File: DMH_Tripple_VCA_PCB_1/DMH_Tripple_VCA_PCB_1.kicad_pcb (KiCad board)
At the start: 2 copper layers, 48 x 175 mm, 88 parts, among them J1 TS_Jack_6.35mm_Sw, J10 TS_Jack_6.35mm_Sw, J100 IDC_02x05, J2 TS_Jack_6.35mm_Sw, J200 IDC_02x05, J3 TS_Jack_6.35mm_Sw, J4 TS_Jack_6.35mm_Sw, J5 TS_Jack_6.35mm_Sw, J50 Conn_01x06, J6 TS_Jack_6.35mm_Sw, J60 Conn_01x06, J7 TS_Jack_6.35mm_Sw, J70 Conn_01x06, J8 TS_Jack_6.35mm_Sw, J9 TS_Jack_6.35mm_Sw, Q1 BC548, Q2 BC548, Q3 BC548, Q4 BC548, Q5 BC548, Q6 BC548, U1 TL074, U2 TL074

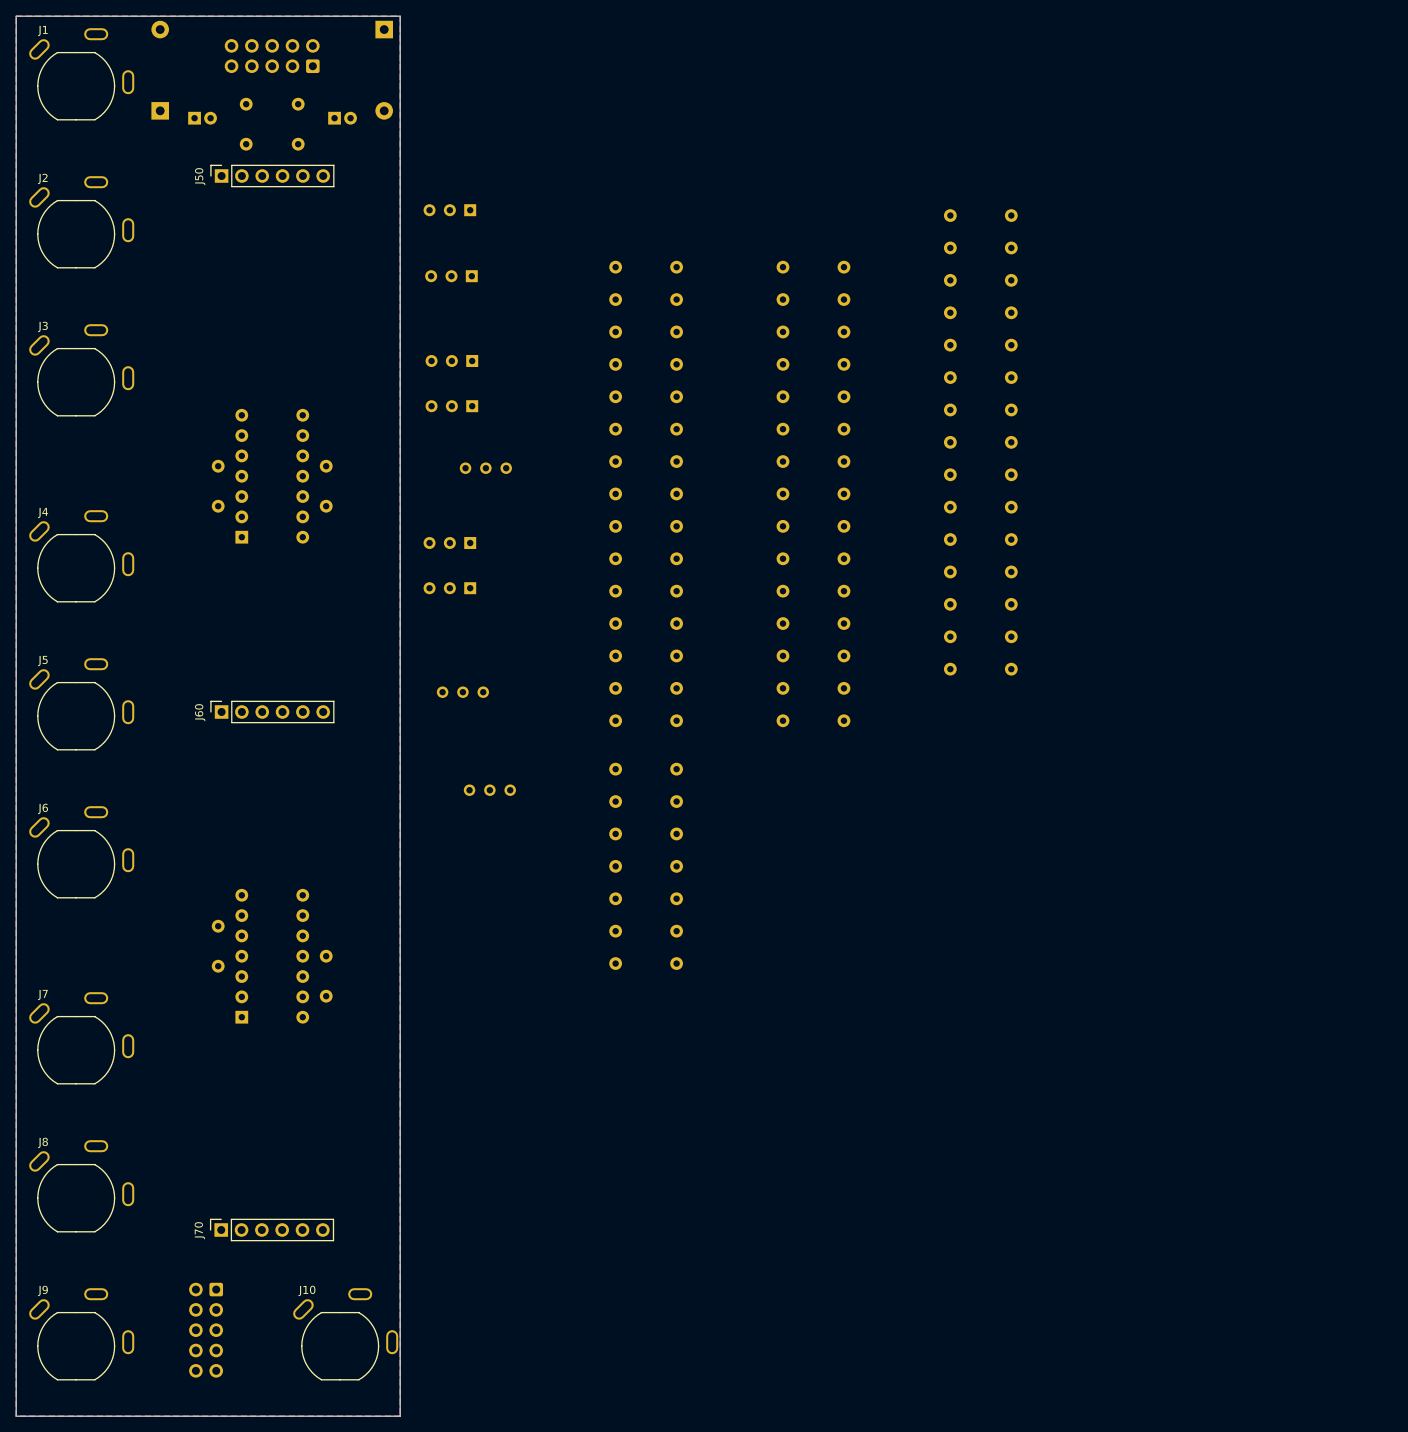
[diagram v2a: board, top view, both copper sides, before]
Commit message: PCB 1 Component placement done
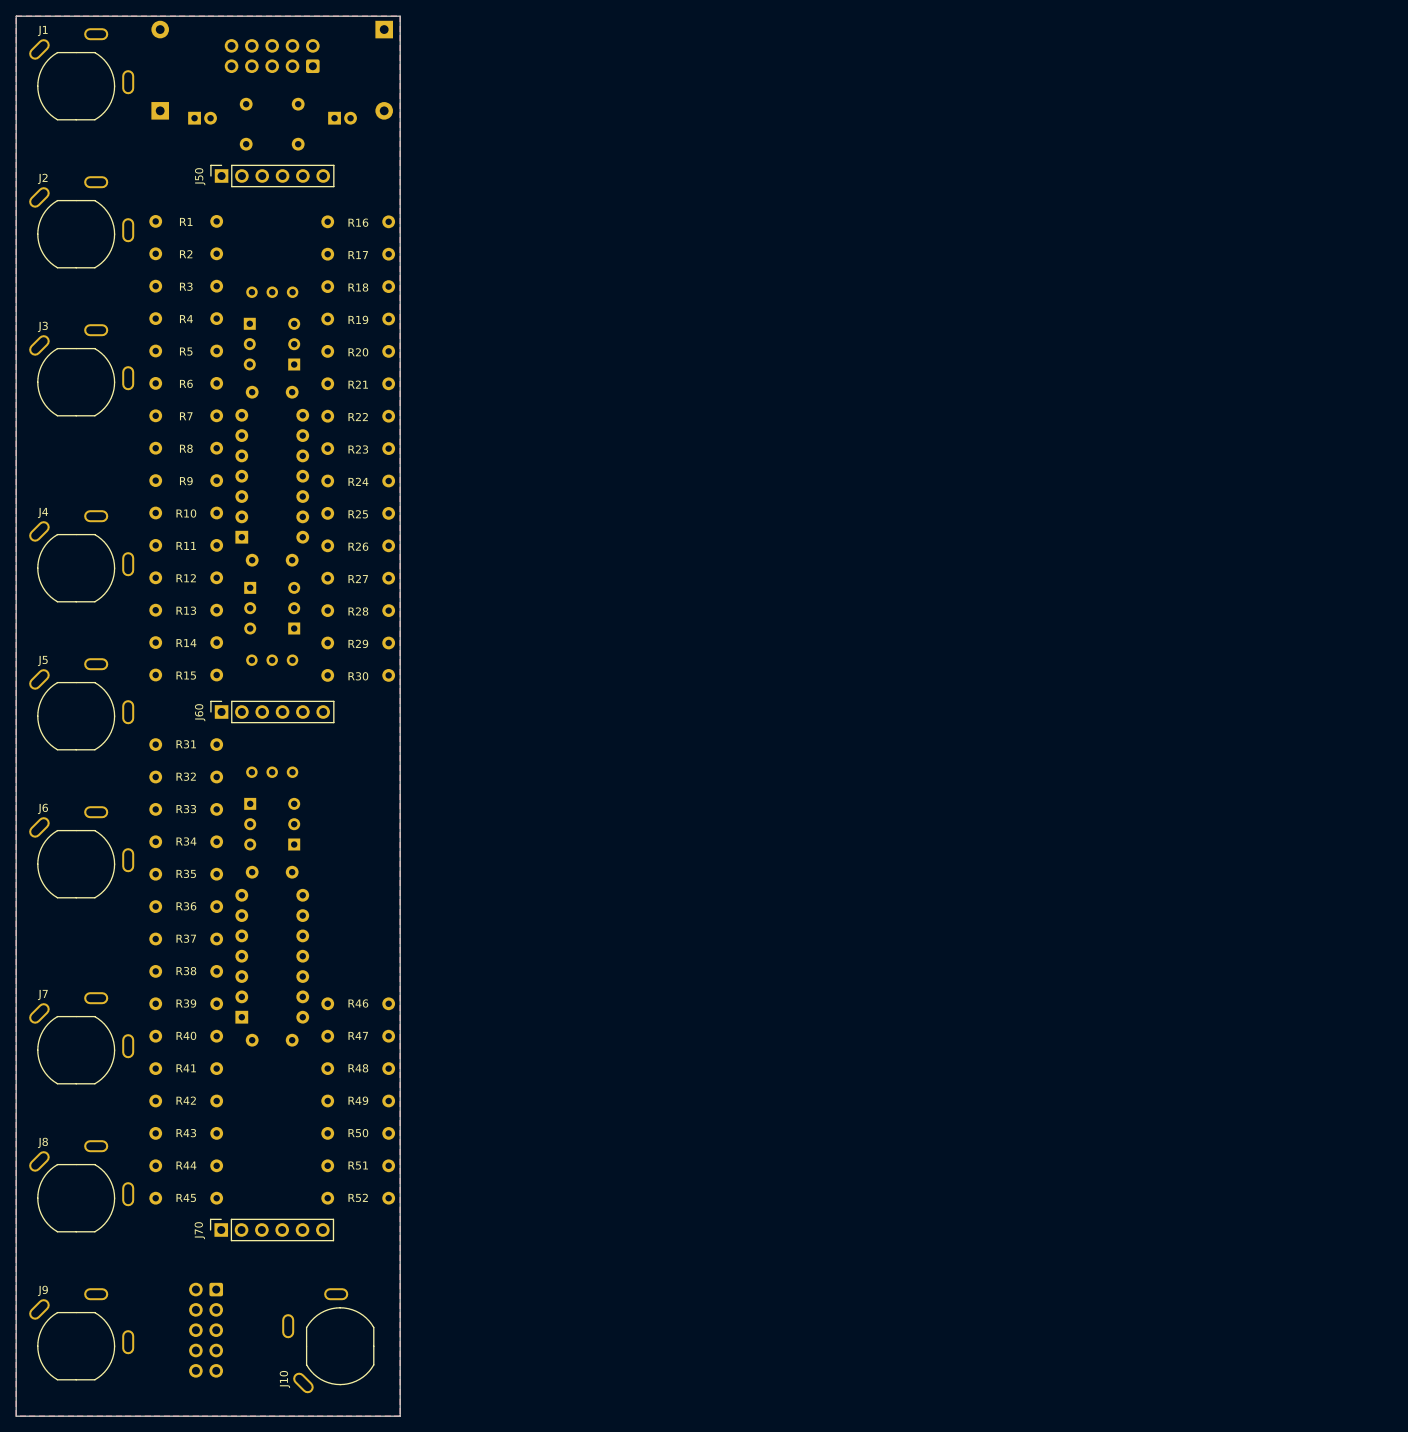
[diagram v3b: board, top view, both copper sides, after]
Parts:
- moved R35 104.7 mm to (68.4, 149.8), turned to 0 degrees
- moved R1 99.3 mm to (76.1, 68.2)
- moved R10 99.3 mm to (76.1, 104.6)
- moved R11 99.3 mm to (76.1, 108.7)
- moved R12 99.3 mm to (76.1, 112.7)
- moved R13 99.3 mm to (76.1, 116.8)
- moved R14 99.3 mm to (76.1, 120.8)
- moved R15 99.3 mm to (76.1, 124.8)
- moved R2 99.3 mm to (76.1, 72.2)
- moved R3 99.3 mm to (76.1, 76.2)
- moved R4 99.3 mm to (76.1, 80.3)
- moved R5 99.3 mm to (76.1, 84.3)
- moved R6 99.3 mm to (76.1, 88.4)
- moved R7 99.3 mm to (76.1, 92.5)
- moved R8 99.3 mm to (76.1, 96.5)
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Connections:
- R13 pad 2: Net-(U1B--) -> Net-(U1A--)
- R14 pad 1: Net-(U1B--) -> Net-(U1A--)
- R15 pad 2: Net-(U1B--) -> Net-(U1A--)
- R18 pad 2: Net-(U1D--) -> Net-(U1C--)
- R19 pad 1: Net-(U1D--) -> Net-(U1C--)
- R21 pad 1: Net-(U1D-+) -> Net-(U1C-+)
- R22 pad 1: Net-(U1D-+) -> Net-(U1C-+)
- R28 pad 2: Net-(U1A--) -> Net-(U1D--)
- R29 pad 1: Net-(U1A--) -> Net-(U1D--)
- R3 pad 2: Net-(U1C--) -> Net-(U1B--)
- R30 pad 2: Net-(U1A--) -> Net-(U1D--)
- R33 pad 2: Net-(U2C--) -> Net-(U2B--)
- R34 pad 1: Net-(U2C--) -> Net-(U2B--)
- R36 pad 1: Net-(U2C-+) -> Net-(U2B-+)
- R37 pad 1: Net-(U2C-+) -> Net-(U2B-+)
- R4 pad 1: Net-(U1C--) -> Net-(U1B--)
- R43 pad 2: Net-(U2B--) -> Net-(U2A--)
- R44 pad 1: Net-(U2B--) -> Net-(U2A--)
- R45 pad 2: Net-(U2B--) -> Net-(U2A--)
- R46 pad 2: Net-(U2A-+) -> Net-(U2C-+)
- R47 pad 1: Net-(U2A-+) -> Net-(U2C-+)
- R48 pad 2: Net-(U2A-+) -> Net-(U2C-+)
- R49 pad 2: Net-(U2A-+) -> Net-(U2C-+)
- R6 pad 1: Net-(U1C-+) -> Net-(U1B-+)
- R7 pad 1: Net-(U1C-+) -> Net-(U1B-+)
- U1 pad 1: Net-(R27-Pad1) -> Net-(R12-Pad1)
- U1 pad 12: Net-(U1D-+) -> GND
- U1 pad 14: Net-(R18-Pad1) -> Net-(R27-Pad1)
- U1 pad 5: GND -> Net-(U1B-+)
- U1 pad 7: Net-(R12-Pad1) -> Net-(R3-Pad1)
- U1 pad 8: Net-(R3-Pad1) -> Net-(R18-Pad1)
- U2 pad 1: Net-(R47-Pad2) -> Net-(R42-Pad1)
- U2 pad 2: GND -> Net-(U2A--)
- U2 pad 3: Net-(U2A-+) -> GND
- U2 pad 5: GND -> Net-(U2B-+)
- U2 pad 7: Net-(R42-Pad1) -> Net-(R33-Pad1)
- U2 pad 8: Net-(R33-Pad1) -> Net-(R47-Pad2)
- U2 pad 9: Net-(U2C--) -> GND

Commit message: Routing ongoing
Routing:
- net +12V: track 0.00 -> 218.4 mm
- net Net-(J200-Pin_1): track 0.00 -> 199.6 mm
- net Net-(J200-Pin_2): track 0.00 -> 176.9 mm
- net Net-(J200-Pin_3): track 0.00 -> 154.1 mm
- net -12V: track 0.00 -> 131.4 mm
- net Net-(J200-Pin_4): track 0.00 -> 126.6 mm
- net /Inputs and Outputs/Mute A Switch: track 0.00 -> 123.5 mm
- net /Inputs and Outputs/Offset A Pot: track 0.00 -> 117.7 mm
- net Net-(J200-Pin_5): track 0.00 -> 102.0 mm
- net /Inputs and Outputs/Mute B Switch: track 0.00 -> 85.8 mm
- net Net-(J200-Pin_6): track 0.00 -> 72.4 mm
- net /Inputs and Outputs/Output C Jack: track 0.00 -> 61.8 mm
- net Net-(J200-Pin_7): track 0.00 -> 49.4 mm
- net /Inputs and Outputs/Input A Jack: track 0.00 -> 48.7 mm
- net /Inputs and Outputs/CV B Jack: track 0.00 -> 48.6 mm
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
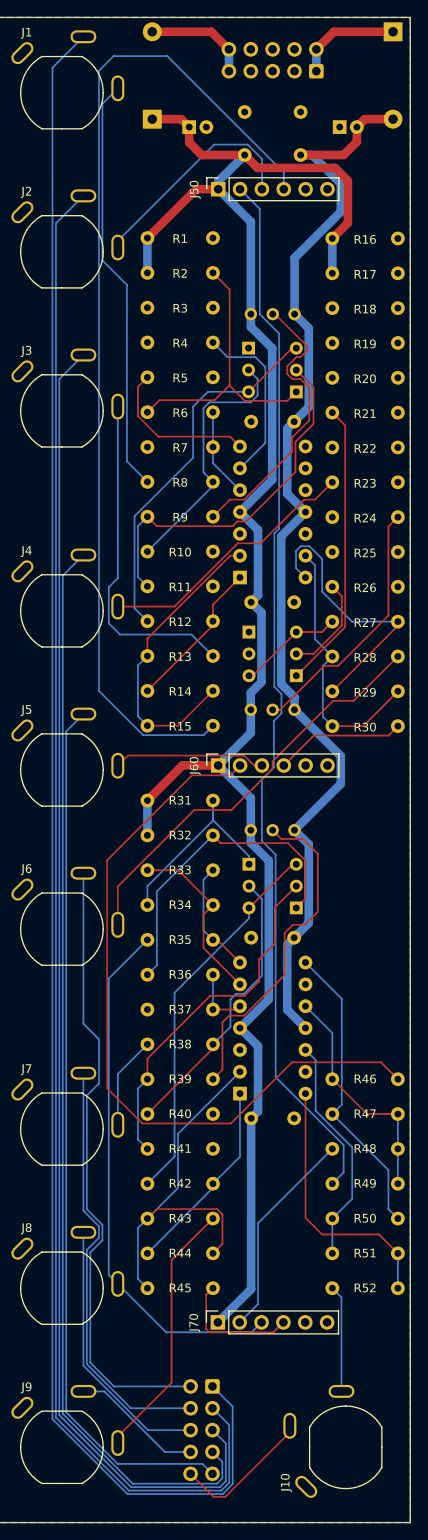
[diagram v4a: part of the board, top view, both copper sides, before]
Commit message: Started routing over with upright resistor fps
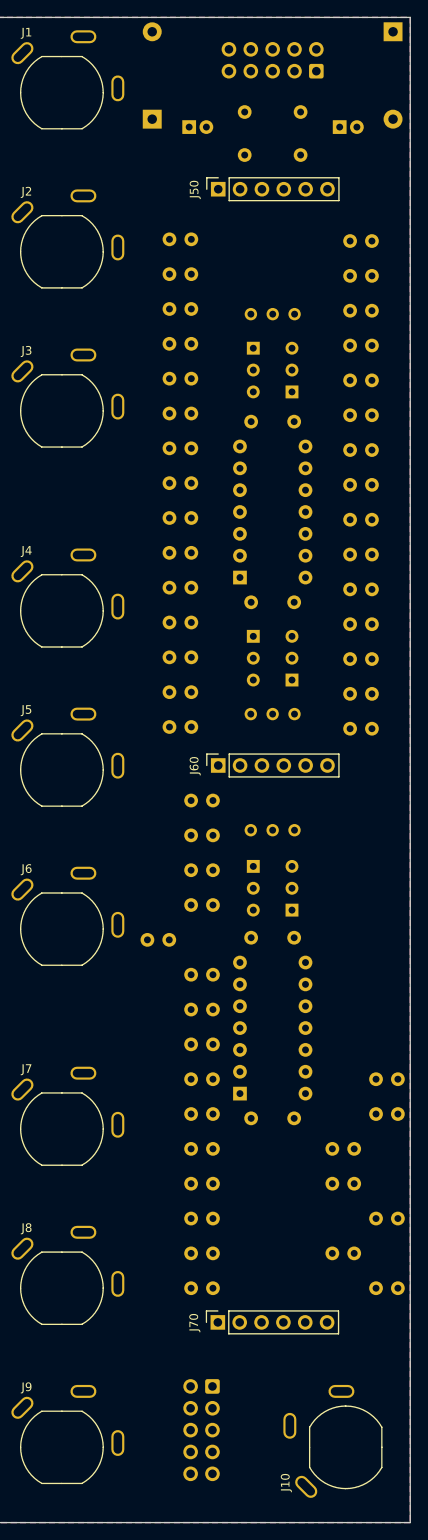
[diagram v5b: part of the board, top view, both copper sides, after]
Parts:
- R1, R10, R11, R12, R13, R14, R15, R16, R17, R18, R19, R2, R20, R21, R22, R23, R24, R25, R26, R27, R28, R29, R3, R30, R31, R32, R33, R34, R35, R36, R37, R38, R39, R4, R40, R41, R42, R43, R44, R45, R46, R47, R48, R49, R5, R50, R51, R52, R6, R7, R8, R9: footprint Resistor_THT:R_Axial_DIN0207_L6.3mm_D2.5mm_P7.62mm_Horizontal -> Resistor_THT:R_Axial_DIN0207_L6.3mm_D2.5mm_P2.54mm_Vertical
- moved R19 3.03 mm to (94.5, 80.7)
- moved R24 3.03 mm to (94.5, 100.9)
- moved R29 3.03 mm to (94.5, 121.2)
- moved R16 3.03 mm to (94.5, 68.5)
- moved R17 3.03 mm to (94.5, 72.5)
- moved R18 3.03 mm to (94.5, 76.6)
- moved R20 3.03 mm to (94.5, 84.7)
- moved R21 3.03 mm to (94.5, 88.8)
- moved R22 3.03 mm to (94.5, 92.8)
- moved R23 3.03 mm to (94.5, 96.8)
- moved R25 3.03 mm to (94.5, 105.0)
- moved R26 3.03 mm to (94.5, 109.0)
- moved R27 3.03 mm to (94.5, 113.0)
- moved R28 3.03 mm to (94.5, 117.1)
- moved R30 3.03 mm to (94.5, 125.2)
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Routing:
- net +12V: track 218.4 -> 0.00 mm
- net Net-(J200-Pin_1): track 199.6 -> 0.00 mm
- net Net-(J200-Pin_2): track 176.9 -> 0.00 mm
- net Net-(J200-Pin_3): track 154.1 -> 0.00 mm
- net -12V: track 131.4 -> 0.00 mm
- net Net-(J200-Pin_4): track 126.6 -> 0.00 mm
- net /Inputs and Outputs/Mute A Switch: track 123.5 -> 0.00 mm
- net /Inputs and Outputs/Offset A Pot: track 117.7 -> 0.00 mm
- net Net-(J200-Pin_5): track 102.0 -> 0.00 mm
- net /Inputs and Outputs/Mute B Switch: track 85.8 -> 0.00 mm
- net Net-(J200-Pin_6): track 72.4 -> 0.00 mm
- net /Inputs and Outputs/Output C Jack: track 61.8 -> 0.00 mm
- net Net-(J200-Pin_7): track 49.4 -> 0.00 mm
- net /Inputs and Outputs/Input A Jack: track 48.7 -> 0.00 mm
- net /Inputs and Outputs/CV B Jack: track 48.6 -> 0.00 mm
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
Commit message: Routed PCB 1
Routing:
- net +12V: track 0.00 -> 202.2 mm
- net Net-(J200-Pin_1): track 0.00 -> 163.2 mm
- net Net-(J200-Pin_2): track 0.00 -> 147.2 mm
- net /Inputs and Outputs/Mute A Switch: track 0.00 -> 145.3 mm
- net -12V: track 0.00 -> 133.5 mm
- net Net-(J200-Pin_3): track 0.00 -> 131.8 mm
- net Net-(J200-Pin_4): track 0.00 -> 112.8 mm
- net Net-(J200-Pin_5): track 0.00 -> 95.1 mm
- net /Inputs and Outputs/Offset A Pot: track 0.00 -> 76.9 mm
- net /Inputs and Outputs/Output B Jack: track 0.00 -> 72.4 mm
- net Net-(J200-Pin_6): track 0.00 -> 64.8 mm
- net /Inputs and Outputs/Output C Jack: track 0.00 -> 60.9 mm
- net /Inputs and Outputs/CV A Jack: track 0.00 -> 58.0 mm
- net /Inputs and Outputs/CV B Jack: track 0.00 -> 55.4 mm
- net Net-(Q3-C): track 0.00 -> 53.7 mm
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
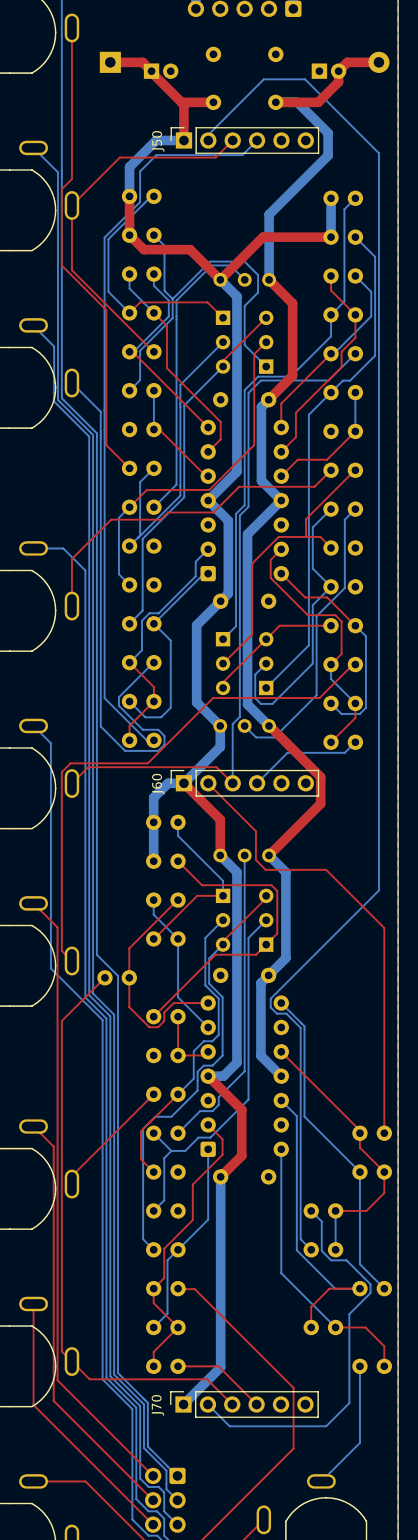
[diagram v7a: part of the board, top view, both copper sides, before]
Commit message: Corrected header locations and placed pcb2 comps
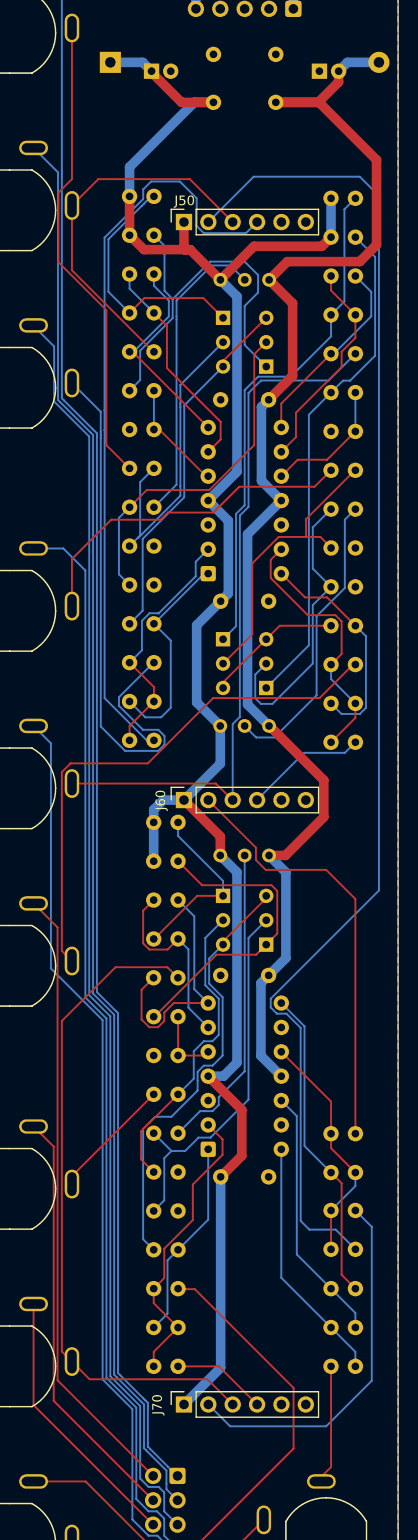
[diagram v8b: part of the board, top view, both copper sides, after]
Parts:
- moved J50 8.50 mm to (76.7, 71.0)
- moved R35 7.61 mm to (76.0, 149.8), turned to 180 degrees
- moved R48 4.61 mm to (94.5, 174.0), turned to 180 degrees
- moved R49 4.61 mm to (94.5, 178.1), turned to 180 degrees
- moved R51 4.61 mm to (94.5, 186.2), turned to 180 degrees
- moved R46 3.02 mm to (94.5, 166.0)
- moved R47 3.02 mm to (94.5, 170.1)
- moved R50 3.02 mm to (94.5, 182.2)
- moved R52 3.02 mm to (94.5, 190.2)
- moved J60 1.75 mm to (76.7, 131.2)
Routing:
- net -12V: track 133.5 -> 144.7 mm
- net /Inputs and Outputs/Output C Jack: track 60.9 -> 69.4 mm
- net Net-(U2D-+): track 32.5 -> 26.9 mm
- net /Inputs and Outputs/Mute A Switch: track 145.3 -> 140.9 mm
- net Net-(U2C-+): track 29.1 -> 24.8 mm
- net Net-(U2B--): track 15.6 -> 19.9 mm
- net Net-(R51-Pad2): track 28.9 -> 25.8 mm
- net /Inputs and Outputs/Mute B Switch: track 47.8 -> 44.8 mm
- net /Inputs and Outputs/Mute C Switch: track 41.1 -> 38.4 mm
- net +12V: track 202.2 -> 204.9 mm
- net Net-(R33-Pad1): track 23.9 -> 25.7 mm
- net /Inputs and Outputs/Offset A Pot: track 76.9 -> 78.3 mm
- net Net-(R47-Pad2): track 34.2 -> 33.0 mm
- net /Inputs and Outputs/Mix Out Jack: track 13.7 -> 12.4 mm
- net /Inputs and Outputs/Output B Jack: track 72.4 -> 73.4 mm
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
